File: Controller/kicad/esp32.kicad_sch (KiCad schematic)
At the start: 9 parts, among them J11 PROG, J12 PI, SW1 RESET, SW2 BOOT, U4 ESP32-WROOM-32D

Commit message: Tweaked board to allow for JLCPCB standard assembly.  Needed fiducials and 5mm rail clearance top and bottom.  Also fixed silkscreen mistake
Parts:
- U4: JLCPCB_CORRECTION (none) -> 0; 0; 90
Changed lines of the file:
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@@
+      (effects (font (size 1.27 1.27)) hide)
+    )
+    (property "JLCPCB_CORRECTION" "0; 0; 90" (id 5) (at 208.28 93.98 0)
       (effects (font (size 1.27 1.27)) hide)
     )

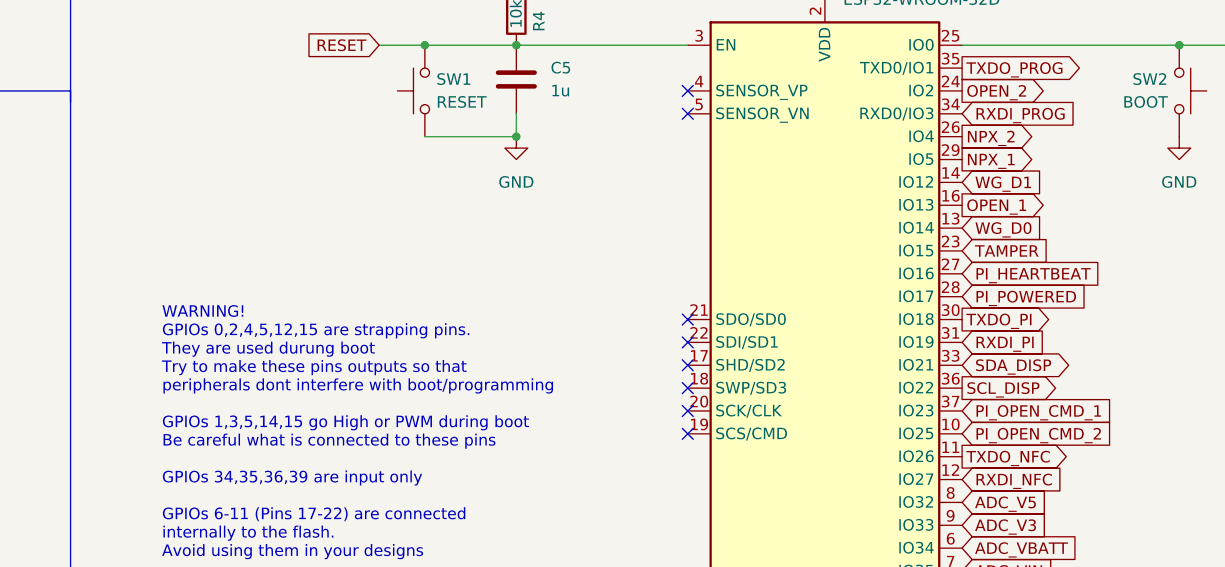
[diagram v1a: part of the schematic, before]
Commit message: Updated schematics based on issues and improvements from the prototype board
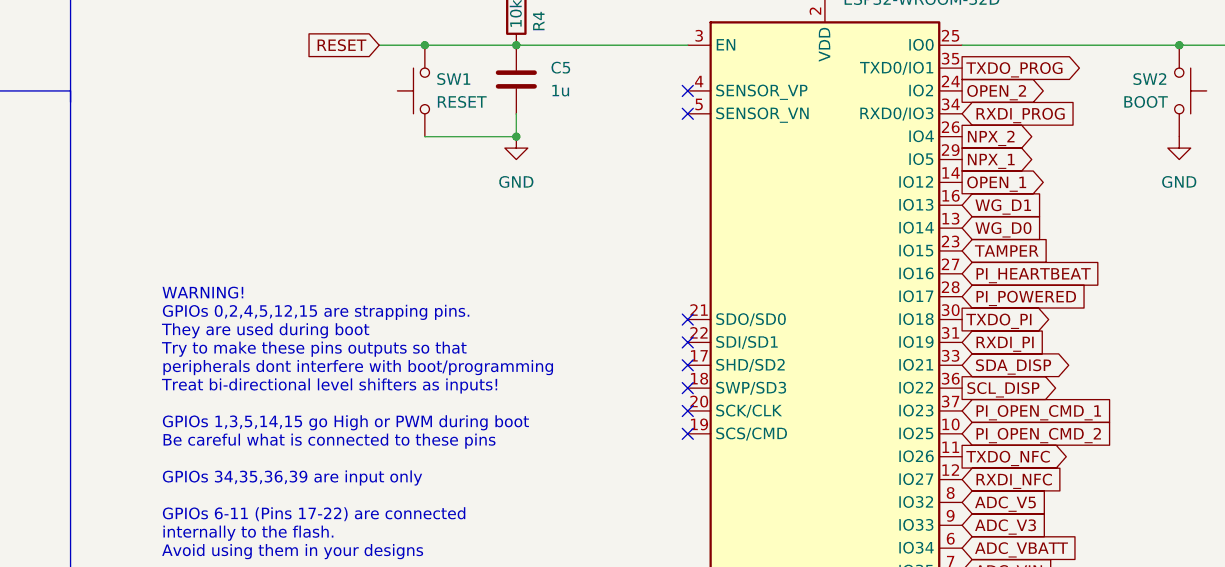
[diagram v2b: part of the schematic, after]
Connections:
- net OPEN_1: now also U4.14 (IO12); no longer U4.16 (IO13)
- net WG_D1: now also U4.16 (IO13); no longer U4.14 (IO12)
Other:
- note added: "WARNING! GPIOs 0,2,4,5,12,15 are strapping pins. They are used during boot Try to make these pins outputs so that peripherals dont interfere with boot/programming Treat bi-directional level shifters as inputs! GPIOs 1,3,5,14,15 go High or PWM during boot Be careful what is connected to these pins GPIOs 34,35,36,39 are input only GPIOs 6-11 (Pins 17-22) are connected internally to the flash. Avoid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"
- note removed: "WARNING! GPIOs 0,2,4,5,12,15 are strapping pins. They are used durung boot Try to make these pins outputs so that peripherals dont interfere with boot/programming GPIOs 1,3,5,14,15 go High or PWM during boot Be careful what is connected to these pins GPIOs 34,35,36,39 are input only GPIOs 6-11 (Pins 17-22) are connected internally to the flash. Avoid using them in your designs"
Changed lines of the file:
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@@
     (effects (font (size 1.27 1.27)) (justify left bottom))
   )
-  (text "WARNING!\nGPIOs 0,2,4,5,12,15 are strapping pins.\nThey are used durung boot\nTry to make these pins outputs so that\nperipherals dont interfere with boot/programming\n\nGPIOs 1,3,5,14,15 go High or PWM during boot\nBe careful what is connected to these pins\n\nGPIOs 34,35,36,39 are input only\n\nGPIOs 6-11 (Pins 17-22) are connected\ninternally to the flash.\nAvoid using them in your designs"
+  (text "WARNING!\nGPIOs 0,2,4,5,12,15 are strapping pins.\nThey are used during boot\nTry to make these pins outputs so that\nperipherals dont interfere with boot/programming\nTreat bi-directional level shifters as inputs!\n\nGPIOs 1,3,5,14,15 go High or PWM during boot\nBe careful what is connected to these pins\n\nGPIOs 34,35,36,39 are input only\n\nGPIOs 6-11 (Pins 17-22) are connected\ninternally to the flash.\nAvoid using them in your designs"
     (at 134.62 120.65 0)
     (effects (font (size 1.27 1.27)) (justify left bottom))
@@
     )
   )
-  (global_label "WG_D1" (shape input) (at 223.52 78.74 0) (fields_autoplaced)
+  (global_label "WG_D1" (shape input) (at 223.52 81.28 0) (fields_autoplaced)
     (effects (font (size 1.27 1.27)) (justify left))
-    (property "Intersheet References" "${INTERSHEET_REFS}" (id 0) (at 232.1017 78.6606 0)
+    (property "Intersheet References" "${INTERSHEET_REFS}" (id 0) (at 232.1017 81.2006 0)
       (effects (font (size 1.27 1.27)) (justify left) hide)
     )
@@
     )
   )
-  (global_label "OPEN_1" (shape output) (at 223.52 81.28 0) (fields_autoplaced)
+  (global_label "OPEN_1" (shape output) (at 223.52 78.74 0) (fields_autoplaced)
     (effects (font (size 1.27 1.27)) (justify left))
-    (property "Intersheet References" "${INTERSHEET_REFS}" (id 0) (at 233.1902 81.2006 0)
+    (property "Intersheet References" "${INTERSHEET_REFS}" (id 0) (at 233.1902 78.6606 0)
       (effects (font (size 1.27 1.27)) (justify left) hide)
     )

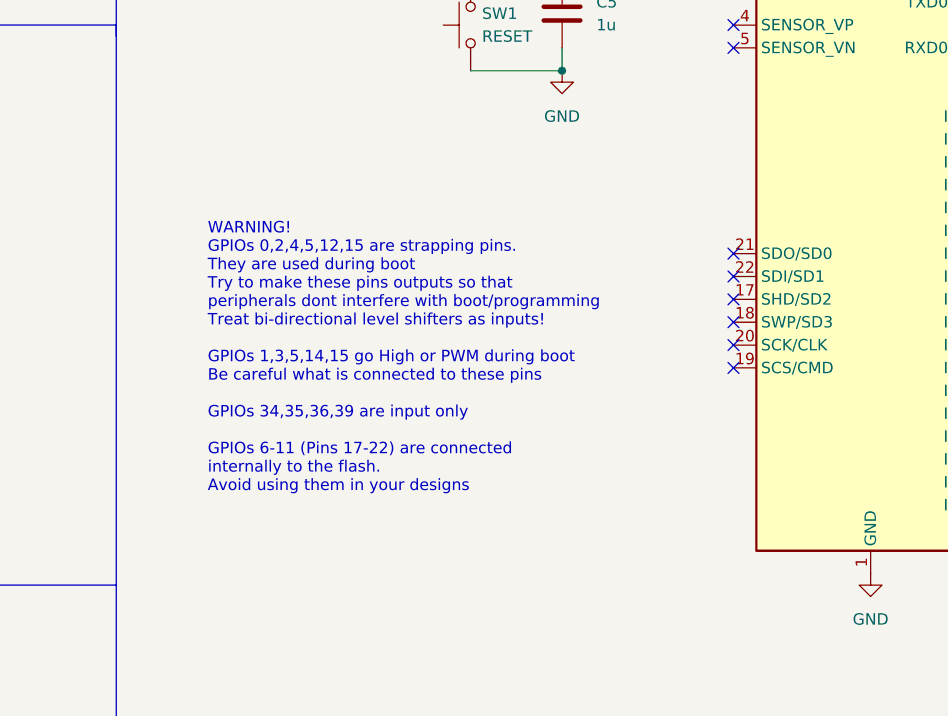
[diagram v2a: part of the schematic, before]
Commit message: Updated schematic to fix issues with V1, including incorrect PCB layout for MP1584
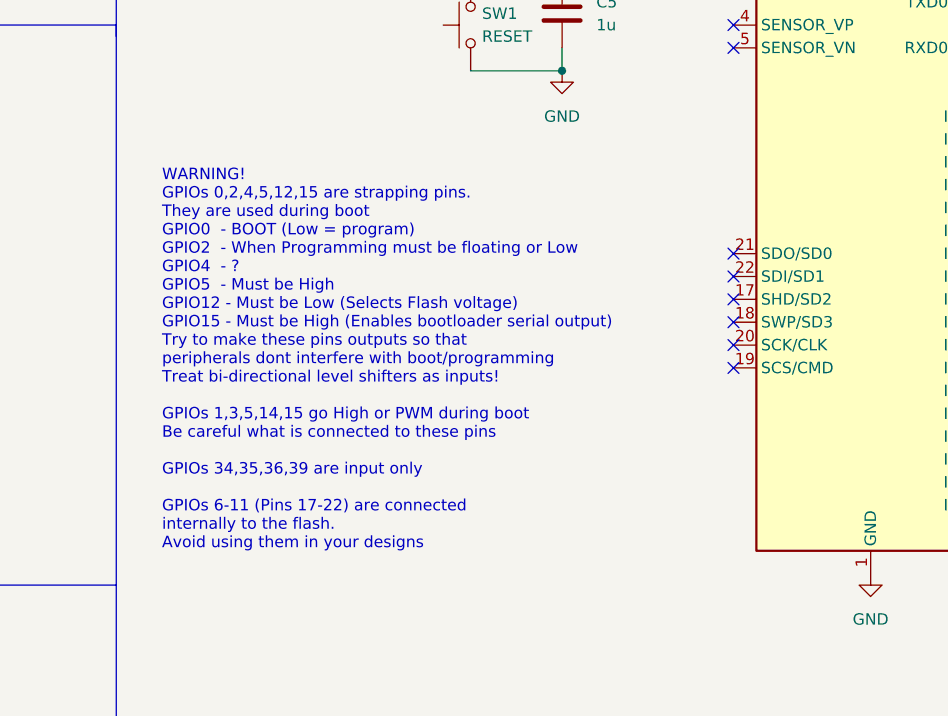
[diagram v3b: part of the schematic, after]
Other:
- note added: "WARNING! GPIOs 0,2,4,5,12,15 are strapping pins. They are used during boot GPIO0 - BOOT (Low = program) GPIO2 - When Programming must be floating or Low GPIO4 - ? GPIO5 - Must be High GPIO12 - Must be Low (Selects Flash voltage) GPIO15 - Must be High (Enables bootloader serial output) Try to make these pins outputs so that peripherals dont interfere with boot/programming Treat bi-directional leve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"
- note removed: "WARNING! GPIOs 0,2,4,5,12,15 are strapping pins. They are used during boot Try to make these pins outputs so that peripherals dont interfere with boot/programming Treat bi-directional level shifters as inputs! GPIOs 1,3,5,14,15 go High or PWM during boot Be careful what is connected to these pins GPIOs 34,35,36,39 are input only GPIOs 6-11 (Pins 17-22) are connected internally to the flash. Avoid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"
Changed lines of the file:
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@@
     (effects (font (size 1.27 1.27)) (justify left bottom))
   )
-  (text "WARNING!\nGPIOs 0,2,4,5,12,15 are strapping pins.\nThey are used during boot\nTry to make these pins outputs so that\nperipherals dont interfere with boot/programming\nTreat bi-directional level shifters as inputs!\n\nGPIOs 1,3,5,14,15 go High or PWM during boot\nBe careful what is connected to these pins\n\nGPIOs 34,35,36,39 are input only\n\nGPIOs 6-11 (Pins 17-22) are connected\ninternally to the flash.\nAvoid using them in your designs"
-    (at 134.62 120.65 0)
+  (text "WARNING!\nGPIOs 0,2,4,5,12,15 are strapping pins.\nThey are used during boot\nGPIO0  - BOOT (Low = program)\nGPIO2  - When Programming must be floating or Low\nGPIO4  - ?\nGPIO5  - Must be High\nGPIO12 - Must be Low (Selects Flash voltage)\nGPIO15 - Must be High (Enables bootloader serial output)\nTry to make these pins outputs so that\nperipherals dont interfere with boot/programming\nTreat bi-directional level shifters as inputs!\n\nGPIOs 1,3,5,14,15 go High or PWM during boot\nBe careful what is connected to these pins\n\nGPIOs 34,35,36,39 are input only\n\nGPIOs 6-11 (Pins 17-22) are connected\ninternally to the flash.\nAvoid using them in your designs"
+    (at 129.54 127 0)
     (effects (font (size 1.27 1.27)) (justify left bottom))
   )

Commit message: Pre-production check-in
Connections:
- net ADC_VBATT: now also U4.7 (IO35); no longer U4.6 (IO34)
- net ADC_VIN: now also U4.6 (IO34); no longer U4.7 (IO35)
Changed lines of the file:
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@@
     )
   )
-  (global_label "ADC_VIN" (shape input) (at 223.52 121.92 0) (fields_autoplaced)
-    (effects (font (size 1.27 1.27)) (justify left))
-    (property "Intersheet References" "${INTERSHEET_REFS}" (id 0) (at 233.5531 121.8406 0)
+  (global_label "ADC_VIN" (shape input) (at 223.52 119.38 0) (fields_autoplaced)
+    (effects (font (size 1.27 1.27)) (justify left))
+    (property "Intersheet References" "${INTERSHEET_REFS}" (id 0) (at 233.5531 119.3006 0)
       (effects (font (size 1.27 1.27)) (justify left) hide)
     )
@@
     )
   )
-  (global_label "ADC_VBATT" (shape input) (at 223.52 119.38 0) (fields_autoplaced)
-    (effects (font (size 1.27 1.27)) (justify left))
-    (property "Intersheet References" "${INTERSHEET_REFS}" (id 0) (at 235.9117 119.3006 0)
+  (global_label "ADC_VBATT" (shape input) (at 223.52 121.92 0) (fields_autoplaced)
+    (effects (font (size 1.27 1.27)) (justify left))
+    (property "Intersheet References" "${INTERSHEET_REFS}" (id 0) (at 235.9117 121.8406 0)
       (effects (font (size 1.27 1.27)) (justify left) hide)
     )
@@
       (effects (font (size 1.27 1.27)) hide)
     )
-    (property "Datasheet" "https://datasheet.lcsc.com/lcsc/2002271431_XKB-Connectivity-TS-1187A-B-A-B_C318884.pdf" (id 3) (at 252.73 68.58 0)
+    (property "Datasheet" "~" (id 3) (at 252.73 68.58 0)
       (effects (font (size 1.27 1.27)) hide)
     )
@@
       (effects (font (size 1.27 1.27)) hide)
     )
-    (property "Datasheet" "https://datasheet.lcsc.com/lcsc/2002271431_XKB-Connectivity-TS-1187A-B-A-B_C318884.pdf" (id 3) (at 158.75 68.58 0)
+    (property "Datasheet" "~" (id 3) (at 158.75 68.58 0)
       (effects (font (size 1.27 1.27)) hide)
     )
@@
       (effects (font (size 1.27 1.27)) hide)
     )
-    (property "Datasheet" "https://datasheet.lcsc.com/lcsc/2110100730_XKB-Connectivity-X9555WV-2x04-6TV01_C2884546.pdf" (id 3) (at 67.31 165.1 0)
-      (effects (font (size 1.27 1.27)) hide)
-    )
+    (property "Datasheet" "~" (id 3) (at 67.31 165.1 0)
+      (effects (font (size 1.27 1.27)) hide)
+    )
